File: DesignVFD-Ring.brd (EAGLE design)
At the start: 70.1 x 70.1 mm, 33 parts, among them IC1 LMR64010XMF/NOPB, IC2 LM340S-05, U1 MAX6920AWP+, U2 LM1084IS-5.0, U3 TPS76325DBVT

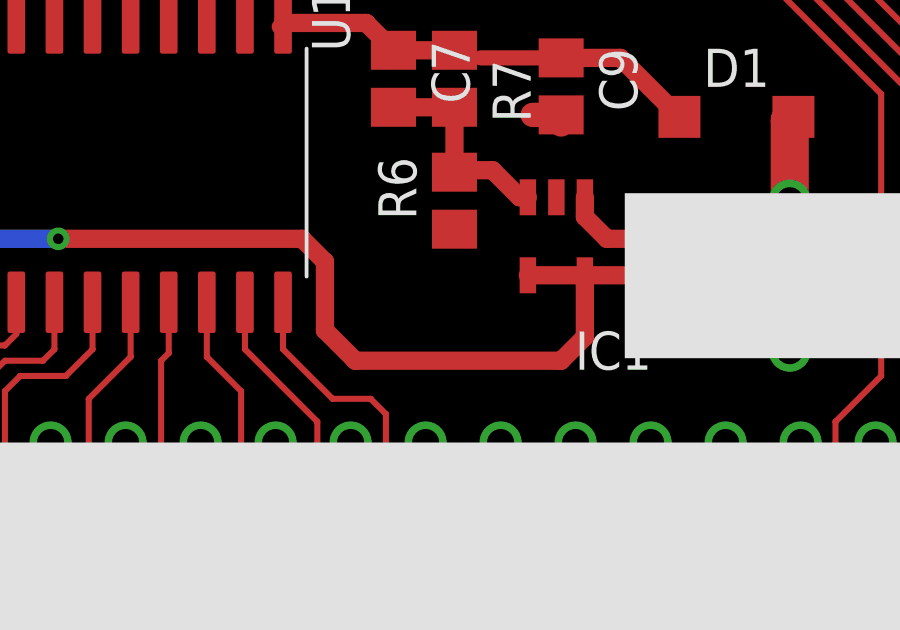
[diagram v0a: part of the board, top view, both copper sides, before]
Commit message: added aesthetic capacitor
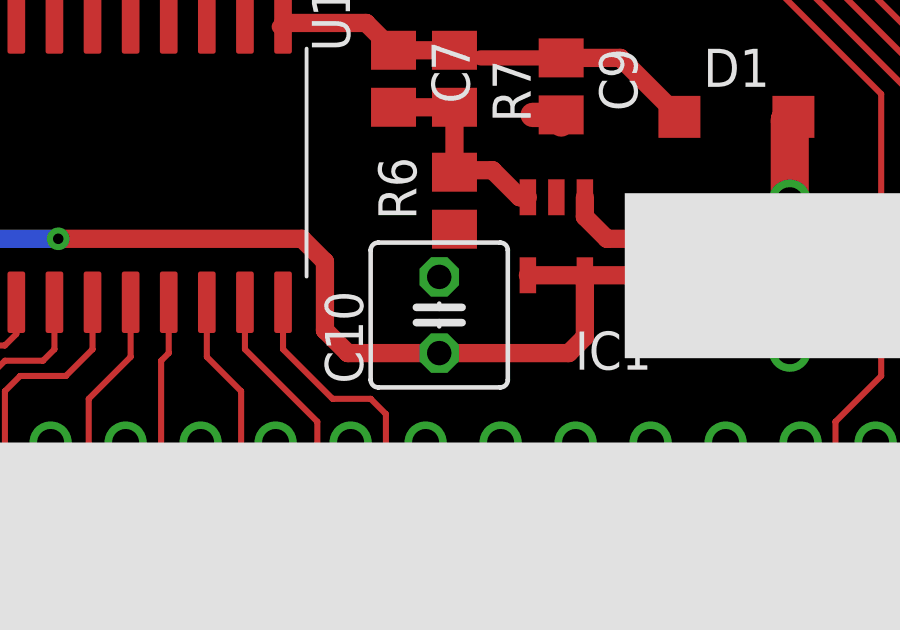
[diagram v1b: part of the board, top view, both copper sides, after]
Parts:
- added C10: (no value), rcl:C025-050X050
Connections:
- net +12V: now also C10.1
- net GND: now also C10.2
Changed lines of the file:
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@@
 <attribute name="VALUE" x="2.286" y="7.493" size="1.27" layer="27"/>
+</element>
+<element name="C10" library="rcl" library_urn="urn:adsk.eagle:library:334" package="C025-050X050" package3d_urn="urn:adsk.eagle:package:23633/1" value="" x="28.702" y="48.26" smashed="yes" rot="R90">
+<attribute name="NAME" x="26.162" y="45.974" size="1.27" layer="25" ratio="10" rot="R90"/>
+<attribute name="SPICEPREFIX" value="C" x="28.702" y="48.26" size="1.778" layer="27" rot="R90" display="off"/>
+<attribute name="VALUE" x="32.512" y="45.974" size="1.27" layer="27" ratio="10" rot="R90"/>
 </element>
 </elements>
@@
 <wire x1="7.62" y1="30.734" x2="8.128" y2="30.734" width="0.2032" layer="16"/>
 <contactref element="JP4" pad="1"/>
+<contactref element="C10" pad="2"/>
 </signal>
 <signal name="T_IGN_INPUT">
@@
 <wire x1="24.892" y1="50.038" x2="24.13" y2="50.8" width="0.6096" layer="1"/>
 <wire x1="24.892" y1="50.038" x2="24.892" y2="47.752" width="0.6096" layer="1"/>
-<wire x1="25.908" y1="46.736" x2="24.892" y2="47.752" width="0.6096" layer="1"/>
+<wire x1="24.892" y1="47.752" x2="25.654" y2="46.99" width="0.6096" layer="1"/>
 <wire x1="33.55623125" y1="49.58458125" x2="40.33141875" y2="49.58458125" width="0.6096" layer="1"/>
 <wire x1="40.33141875" y1="49.58458125" x2="40.386" y2="49.53" width="0.6096" layer="1"/>
 <wire x1="40.386" y1="49.53" x2="40.386" y2="47.07" width="0.6096" layer="1"/>
-<wire x1="33.55623125" y1="49.58458125" x2="33.55623125" y2="47.52623125" width="0.6096" layer="1"/>
-<wire x1="33.55623125" y1="47.52623125" x2="32.766" y2="46.736" width="0.6096" layer="1"/>
-<wire x1="32.766" y1="46.736" x2="25.908" y2="46.736" width="0.6096" layer="1"/>
+<wire x1="33.55623125" y1="47.52623125" x2="33.55623125" y2="49.58458125" width="0.6096" layer="1"/>
 <wire x1="31.656234375" y1="49.58458125" x2="33.55623125" y2="49.58458125" width="0.6096" layer="1"/>
+<contactref element="C10" pad="1"/>
+<wire x1="28.702" y1="46.99" x2="25.654" y2="46.99" width="0.6096" layer="1"/>
+<wire x1="33.02" y1="46.99" x2="33.55623125" y2="47.52623125" width="0.6096" layer="1"/>
+<wire x1="28.702" y1="46.99" x2="33.02" y2="46.99" width="0.6096" layer="1"/>
 </signal>
 <signal name="N$7">

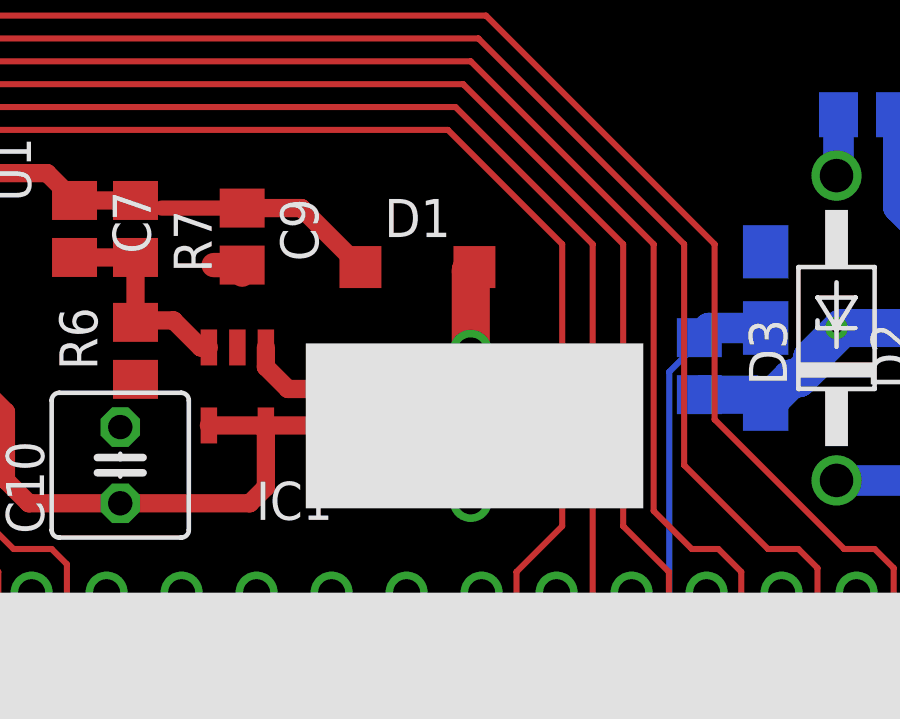
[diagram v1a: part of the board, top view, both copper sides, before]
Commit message: rotated inductor
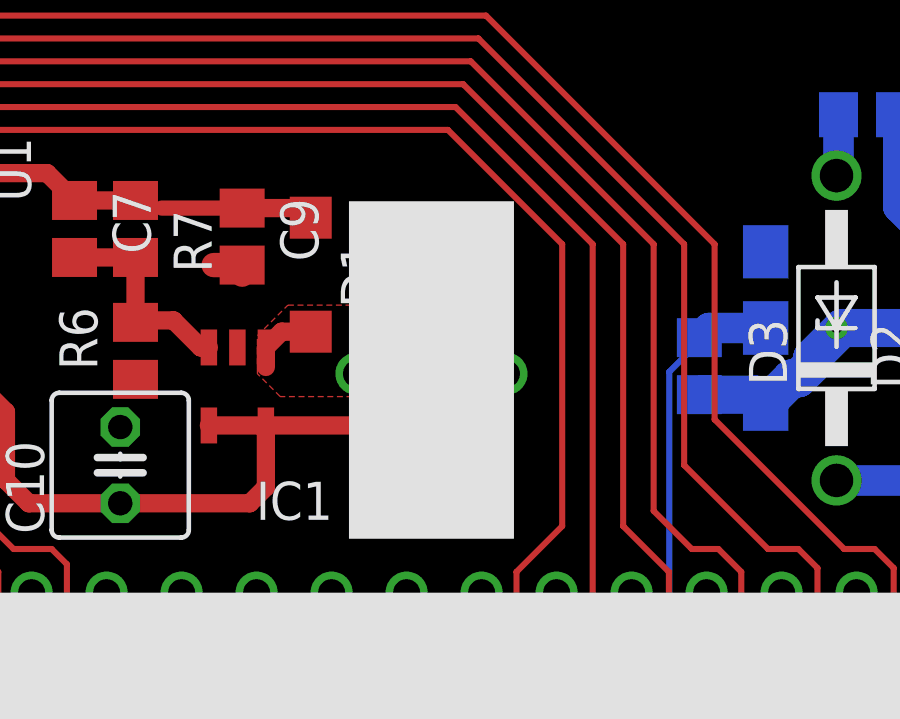
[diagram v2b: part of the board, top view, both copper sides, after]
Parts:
- moved U$1 3.89 mm to (36.6, 51.3), turned to 0 degrees
- moved D1 3.57 mm to (35.1, 54.6), turned to 270 degrees
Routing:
- net N$6: track 11.6 -> 2.36 mm
- net +24V: track 14.7 -> 12.4 mm
- added copper zone on layer 1, net N$6
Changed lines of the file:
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@@
 <layer number="45" name="Holes" color="7" fill="1" visible="yes" active="yes"/>
 <layer number="46" name="Milling" color="3" fill="1" visible="no" active="yes"/>
-<layer number="47" name="Measures" color="7" fill="1" visible="no" active="yes"/>
+<layer number="47" name="Measures" color="7" fill="1" visible="yes" active="yes"/>
 <layer number="48" name="Document" color="7" fill="1" visible="no" active="yes"/>
 <layer number="49" name="Reference" color="7" fill="1" visible="no" active="yes"/>
@@
 <attribute name="VALUE" x="30.226" y="57.15" size="1.27" layer="27" rot="R270"/>
 </element>
-<element name="D1" library="diode" library_urn="urn:adsk.eagle:library:210" package="SOD123" package3d_urn="urn:adsk.eagle:package:43420/1" value="MBR0520LT" x="38.608" y="54.864" smashed="yes">
-<attribute name="NAME" x="37.508" y="55.864" size="1.27" layer="25"/>
-<attribute name="VALUE" x="37.508" y="52.564" size="1.27" layer="27"/>
+<element name="D1" library="diode" library_urn="urn:adsk.eagle:library:210" package="SOD123" package3d_urn="urn:adsk.eagle:package:43420/1" value="MBR0520LT" x="35.052" y="54.61" smashed="yes" rot="R270">
+<attribute name="NAME" x="36.052" y="55.71" size="1.27" layer="25" rot="R270"/>
+<attribute name="VALUE" x="32.752" y="55.71" size="1.27" layer="27" rot="R270"/>
 </element>
 <element name="D2" library="diode" library_urn="urn:adsk.eagle:library:210" package="DO41-10" package3d_urn="urn:adsk.eagle:package:43336/1" value="1N4004" x="56.642" y="52.832" smashed="yes" rot="R90">
@@
 <attribute name="VALUE" x="26.67" y="56.769" size="1.27" layer="27" rot="R270"/>
 </element>
-<element name="U$1" library="FormE" package="732-1416-ND" value="10uF" x="40.386" y="52.07" smashed="yes" rot="R270"/>
+<element name="U$1" library="FormE" package="732-1416-ND" value="10uF" x="36.576" y="51.308" smashed="yes"/>
 <element name="U$2" library="FormE" package="IVL2-7/5" value="IVL2-7/5" x="15.748" y="16.51" smashed="yes"/>
 <element name="U1" library="MAX6920AWP_" package="SOIC127P1032X265-20N" value="MAX6920AWP+" x="17.78" y="53.34" smashed="yes" rot="R270">
@@
 <wire x1="33.55623125" y1="49.58458125" x2="40.33141875" y2="49.58458125" width="0.6096" layer="1"/>
 <wire x1="40.33141875" y1="49.58458125" x2="40.386" y2="49.53" width="0.6096" layer="1"/>
-<wire x1="40.386" y1="49.53" x2="40.386" y2="47.07" width="0.6096" layer="1"/>
+<wire x1="40.386" y1="49.53" x2="41.576" y2="51.308" width="0.6096" layer="1"/>
 <wire x1="33.55623125" y1="47.52623125" x2="33.55623125" y2="49.58458125" width="0.6096" layer="1"/>
 <wire x1="31.656234375" y1="49.58458125" x2="33.55623125" y2="49.58458125" width="0.6096" layer="1"/>
@@
 <contactref element="U$1" pad="P$1"/>
 <contactref element="D1" pad="A"/>
-<wire x1="40.508" y1="54.864" x2="40.386" y2="54.742" width="1.27" layer="1"/>
-<wire x1="40.386" y1="54.742" x2="40.386" y2="52.07" width="1.27" layer="1"/>
 <wire x1="33.55623125" y1="52.18458125" x2="33.55623125" y2="51.53376875" width="0.6096" layer="1"/>
-<wire x1="33.55623125" y1="51.53376875" x2="34.29" y2="50.8" width="0.6096" layer="1"/>
-<wire x1="34.29" y1="50.8" x2="39.878" y2="50.8" width="0.6096" layer="1"/>
-<wire x1="39.878" y1="50.8" x2="40.386" y2="51.308" width="0.6096" layer="1"/>
-<wire x1="40.386" y1="51.308" x2="40.386" y2="52.07" width="0.6096" layer="1"/>
+<wire x1="33.55623125" y1="52.18458125" x2="34.08165" y2="52.71" width="0.6096" layer="1"/>
+<wire x1="34.08165" y1="52.71" x2="35.052" y2="52.71" width="0.6096" layer="1"/>
+<polygon width="0.254" layer="1" thermals="no">
+<vertex x="33.274" y="51.308"/>
+<vertex x="33.274" y="52.578"/>
+<vertex x="34.29" y="53.594"/>
+<vertex x="36.576" y="53.594"/>
+<vertex x="37.592" y="52.578"/>
+<vertex x="37.592" y="51.054"/>
+<vertex x="37.084" y="50.546"/>
+<vertex x="34.036" y="50.546"/>
+</polygon>
 </signal>
 <signal name="+24V">
@@
 <wire x1="23.368" y1="57.868" x2="23.495" y2="57.995" width="0.508" layer="1"/>
 <wire x1="32.766" y1="56.83" x2="30.082" y2="56.83" width="0.508" layer="1"/>
-<wire x1="36.708" y1="54.864" x2="34.742" y2="56.83" width="0.6096" layer="1"/>
+<wire x1="35.052" y1="56.51" x2="34.742" y2="56.83" width="0.6096" layer="1"/>
 <wire x1="34.742" y1="56.83" x2="32.766" y2="56.83" width="0.6096" layer="1"/>
 <wire x1="23.495" y1="57.995" x2="26.267" y2="57.995" width="0.6096" layer="1"/>

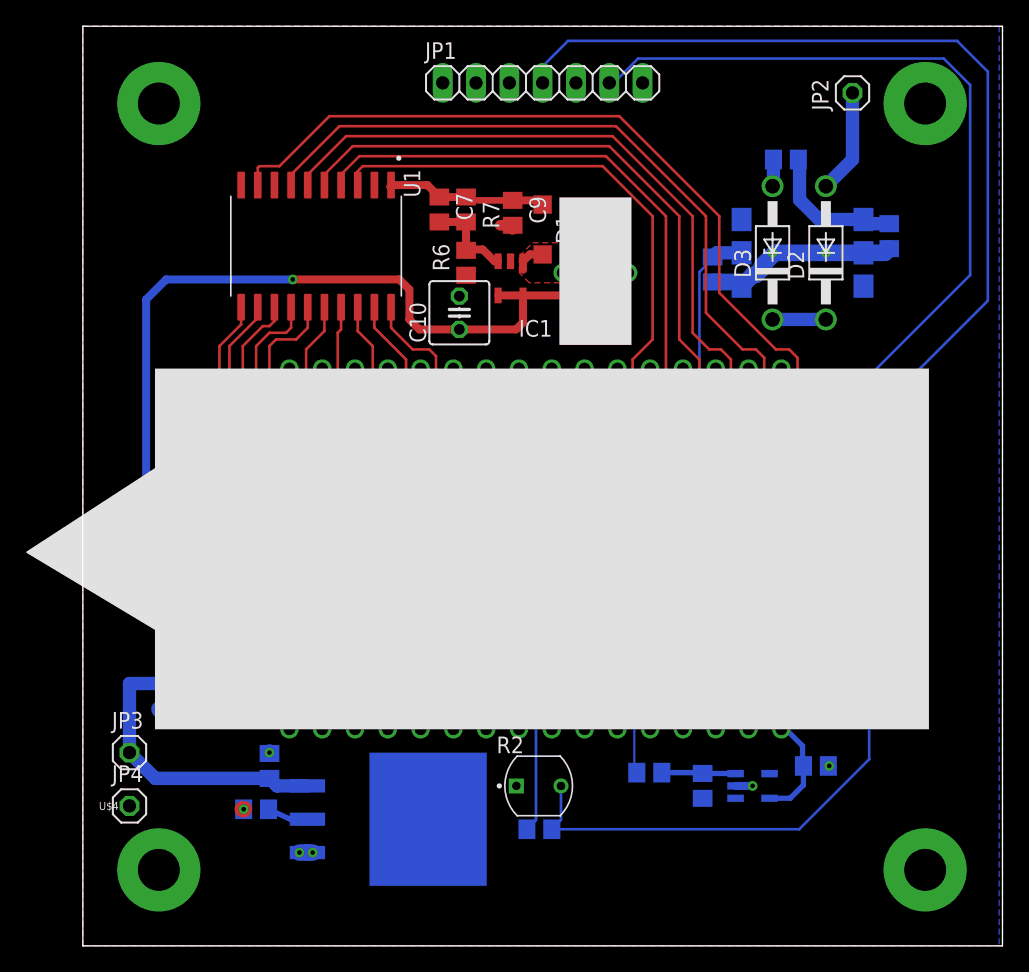
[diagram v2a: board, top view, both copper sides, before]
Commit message: created and added logo, removed board markings
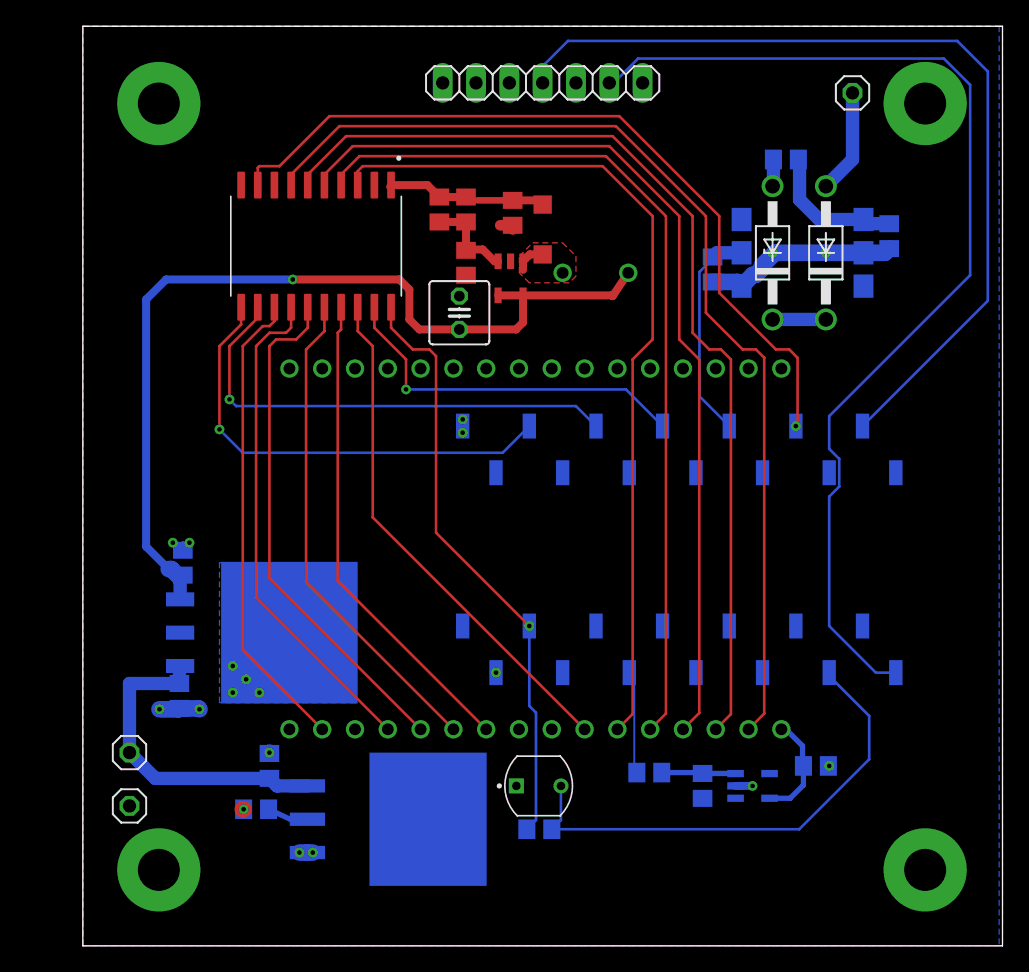
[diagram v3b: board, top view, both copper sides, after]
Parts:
- U$1: value 10uF -> 10uH
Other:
- board text added: "E:/Git/RetroFuture-Dash/logo.bmp"
